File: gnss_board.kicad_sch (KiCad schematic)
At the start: 37 parts, among them J1 Conn_01x10_Pin, U1 H1102NL, U2 LAN8710A

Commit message: Schematic of the power supply with footprings
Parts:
- added C10: 2.2uF, symbol Device:C_Small
- added C11, C13, C14, C9: 100nF, symbol Device:C_Small
- added C12, C8: 22uF, symbol Device:C_Small
- added C15: 22uF/6.3V/20%/X5R/C0603, OLIMEX_RLC-FP:C_0603_5MIL_DWS, symbol ESP32-PoE_Rev_L1:C
- added C16: 12pF, Capacitor_SMD:C_0805_2012Metric, symbol Device:C_Small
- added C17: 470uF, Capacitor_THT:CP_Radial_D6.3mm_P2.50mm, symbol Device:C_Polarized
- added C18: 100nF, Capacitor_SMD:C_0805_2012Metric, symbol Device:C_Small
- added C19: 220pF, Capacitor_SMD:C_0805_2012Metric, symbol Device:C_Small
- added C7: 15uF, Capacitor_THT:CP_Radial_D6.3mm_P2.50mm, symbol Device:C_Polarized
- added D3: SS510, symbol Device:D_Schottky
- added FET1: WPM2015-3/TR, OLIMEX_Transistors-FP:SOT23, symbol ESP32-PoE_Rev_L1:P-MOS+DIOD
- added L2: 33uH, gnss_board:INDPM120120X800N, symbol Device:L
- added R21, R22: 4.42K, symbol Device:R
- added R23: 24.9K, symbol Device:R
- added R24: 0.03R, Resistor_SMD:R_1206_3216Metric, symbol Device:R
- added R25: 4.7K, Resistor_SMD:R_2512_6332Metric, symbol Device:R
- added R26: 10k/R0402, OLIMEX_RLC-FP:R_0402_5MIL_DWS, symbol ESP32-PoE_Rev_L1:R
- added R27: 1k/R0402, OLIMEX_RLC-FP:R_0402_5MIL_DWS, symbol ESP32-PoE_Rev_L1:R
- added R28: 301K, Resistor_SMD:R_0805_2012Metric, symbol Device:R
- added R29: 95.3K, Resistor_SMD:R_0805_2012Metric, symbol Device:R
- added R30: 4.7R, Resistor_SMD:R_0805_2012Metric, symbol Device:R
- added R31: 22R, Resistor_SMD:R_0805_2012Metric, symbol Device:R
- added T1: LMUN2211LT1G(SOT-23), OLIMEX_Transistors-FP:SOT23, symbol ESP32-PoE_Rev_L1:LMUN2211LT1G(SOT-23)
- added U3: TPS2375D, GNSS Board:SOIC127P599X175-8N, symbol gnss_board:TPS2375D
- added U4: TX4138(ESOIC-8), Package_SO:SOIC-8-1EP_3.9x4.9mm_P1.27mm_EP2.29x3mm_ThermalVias, symbol gnss_board:TX4138(ESOIC-8)
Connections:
- net +3.3VLAN: now also U2.12 (VDDIO), C8.1, C9.2, FET1.3
- net GND: now also C10.1, C11.1, C12.1, C13.1, C14.1, C17.2, C19.2, C7.2, C8.2, C9.1, D3.2 (A), R25.2, R29.2, T1.2 (E), U3.5 (RTN), U4.4 (GND)
- net VDD1A: now also U2.1 (VDD2A), U2.27 (VDD1A), C12.2, C13.2, C14.2
- net VIN+: now also C7.1, R23.2, R24.1, R25.1, U3.8 (VDD), U4.3 (Vin)
- net VIN-: now also R21.2, R22.2, U3.4 (VSS)
- net at U2.6 (VDDCR): now also C10.2, C11.2
- new net: R30.1, U4.8 (BS)
- new net: C18.1, R30.2
- new net: C18.2, D3.1 (K), L2.1, R31.1, U4.1 (SW)
- new net: R24.2, U4.2 (ILIM), U4.9 (ILIM)
- new net: C16.2, R28.2, R29.1, U4.5 (FB)
- new net: R21.1, U3.2 (CLASS)
- new net: C19.1, R31.2
- new net: R22.1, U3.1 (ILIM)
- new net: C15.2, FET1.1, R26.2, R27.1
- new net: R23.1, U3.3 (DET)
- new net: R27.2, T1.3 (C)
- new net +3.3V: C15.1, C16.1, C17.1, FET1.2, L2.2, R26.1, R28.1
- new net GPIO12\PHY_PWR: T1.1 (B)
- new net PSU_EN: U3.6 (PG), U4.6 (EN)
- no-connect marks 11 -> 13
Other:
- note added: "PoE PDC"
- note added: "Power Supply"
- moved on the sheet: C6, D5, D6, R10, R11, R12, R13, R14, R15, R16, R17, R18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

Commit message: Slowly grinding
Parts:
- R21: footprint (none) -> Resistor_SMD:R_0805_2012Metric; Info (none) -> 1%/R0805
- R22: value 4.42K -> 180K; footprint (none) -> Resistor_SMD:R_0805_2012Metric; Info (none) -> 1%/R0805
- R23: Info (none) -> 1%/R0805
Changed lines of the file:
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@@
 	)
 	(junction
-		(at 69.85 130.81)
-		(diameter 0)
-		(color 0 0 0 0)
-	)
-	(junction
 		(at 100.33 33.02)
 		(diameter 0)
@@
 	)
 	(junction
+		(at 71.12 130.81)
+		(diameter 0)
+		(color 0 0 0 0)
+	)
+	(junction
+		(at 71.12 146.05)
+		(diameter 0)
+		(color 0 0 0 0)
+	)
+	(junction
 		(at 335.28 30.48)
 		(diameter 0)
@@
 	)
 	(junction
-		(at 69.85 146.05)
-		(diameter 0)
-		(color 0 0 0 0)
-	)
-	(junction
 		(at 257.81 45.72)
 		(diameter 0)
@@
 	(wire
 		(pts
-			(xy 55.88 146.05) (xy 69.85 146.05)
+			(xy 55.88 146.05) (xy 71.12 146.05)
 		)
 		(stroke
@@
 	(wire
 		(pts
-			(xy 67.31 125.73) (xy 69.85 125.73)
+			(xy 67.31 125.73) (xy 71.12 125.73)
 		)
 		(stroke
@@
 	(wire
 		(pts
-			(xy 69.85 125.73) (xy 69.85 130.81)
+			(xy 71.12 125.73) (xy 71.12 130.81)
 		)
 		(stroke
@@
 	(wire
 		(pts
-			(xy 69.85 130.81) (xy 69.85 146.05)
+			(xy 71.12 130.81) (xy 71.12 146.05)
 		)
 		(stroke
@@
 	(wire
 		(pts
-			(xy 69.85 146.05) (xy 76.2 146.05)
-		)
-		(stroke
-			(width 0)
-			(type default)
-		)
-	)
-	(wire
-		(pts
 			(xy 48.26 43.18) (xy 53.34 43.18)
 		)
@@
 	(wire
 		(pts
-			(xy 67.31 130.81) (xy 69.85 130.81)
+			(xy 67.31 130.81) (xy 71.12 130.81)
 		)
 		(stroke
@@
 	(wire
 		(pts
+			(xy 71.12 146.05) (xy 76.2 146.05)
+		)
+		(stroke
+			(width 0)
+			(type default)
+		)
+	)
+	(wire
+		(pts
 			(xy 54.61 59.69) (xy 54.61 54.61)
 		)
@@
 			(effects
 				(font
-					(size 1.27 1.27)
+					(size 1 1)
 				)
 			)
 		)
-		(property "Footprint" ""
+		(property "Footprint" "Resistor_SMD:R_0805_2012Metric"
 			(at 63.5 127.508 90)
 			(effects
@@
 			)
 		)
+		(property "Info" "1%/R0805"
+			(at 68.326 124.968 90)
+			(effects
+				(font
+					(size 0.5 0.5)
+				)
+			)
+		)
 		(pin "2"
 		)
@@
 			)
 		)
-		(property "Value" "4.42K"
+		(property "Value" "180K"
 			(at 63.5 130.81 90)
 			(effects
 				(font
-					(size 1.27 1.27)
+					(size 1 1)
 				)
 			)
 		)
-		(property "Footprint" ""
+		(property "Footprint" "Resistor_SMD:R_0805_2012Metric"
 			(at 63.5 132.588 90)
 			(effects
@@
 			)
 		)
+		(property "Info" "1%/R0805"
+			(at 68.326 130.048 90)
+			(effects
+				(font
+					(size 0.5 0.5)
+				)
+			)
+		)
 		(pin "2"
 		)
@@
 			(effects
 				(font
-					(size 1.27 1.27)
+					(size 1 1)
 				)
 			)
@@
 			)
 		)
+		(property "Info" "1%/R0805"
+			(at 68.326 127.508 90)
+			(effects
+				(font
+					(size 0.5 0.5)
+				)
+			)
+		)

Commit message: Add footprints and arange components around
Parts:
- C1, C2, C3, C4: footprint (none) -> Capacitor_SMD:C_1206_3216Metric
- C10, C11, C12, C13: footprint (none) -> Capacitor_SMD:C_0805_2012Metric; Info (none) -> 10%/C0805
- C14, C9: footprint (none) -> Capacitor_SMD:C_0805_2012Metric; Info (none) -> 16V/10%/C0805
- C15: value 22uF/6.3V/20%/X5R/C0603 -> 22uF; footprint OLIMEX_RLC-FP:C_0603_5MIL_DWS -> Capacitor_SMD:C_0805_2012Metric; Fieldname 1 Value 1 -> (none); Fieldname2 Value2 -> (none); Fieldname3 Value3 -> (none); Info (none) -> 6.3V/20%/C0805
- C6: footprint (none) -> Capacitor_SMD:C_0805_2012Metric; Info (none) -> 6.3V/20%/C0805
- C8: footprint (none) -> Capacitor_SMD:C_0805_2012Metric; Field5 (none) -> 6.3V/20%/C0805
- D1: footprint MB10S:SOIC245P670X290-4N -> GNSS Board:SOIC245P670X290-4N
- D2: footprint MB10S:SOIC245P670X290-4N -> gnss_board:SOIC245P670X290-4N
- D5: Info (none) -> Yellow/D0805
- D6: footprint (none) -> LED_SMD:LED_0805_2012Metric; Info (none) -> Green/D0805
- FET1: footprint OLIMEX_Transistors-FP:SOT23 -> Package_TO_SOT_SMD:SOT-23_Handsoldering
- J1: footprint (none) -> Connector_JST:JST_SH_BM10B-SRSS-TB_1x10-1MP_P1.00mm_Vertical
- L1: value FB0805/600R/2A -> FB0805; footprint OLIMEX_RLC-FP:L_0805_5MIL_DWS -> Inductor_SMD:L_0805_2012Metric_Pad1.15x1.40mm_HandSolder; Fieldname 1 Value 1 -> (none); Fieldname2 Value2 -> (none); Fieldname3 Value3 -> (none); Info (none) -> 600R/2A
- R1, R2, R3, R4: footprint (none) -> Resistor_SMD:R_0805_2012Metric; Info 75V/100mW/0603/C4275 -> 1%/R0805
- R10, R12, R13, R14, R15, R16, R17, R18, R19, R9: value R -> 2.2K; footprint (none) -> Resistor_SMD:R_0805_2012Metric; Info (none) -> 5%/R0805
- R11: footprint (none) -> Resistor_SMD:R_0805_2012Metric; Info (none) -> 1%/R0805
- R20: footprint (none) -> Resistor_SMD:R_0805_2012Metric; Info (none) -> 5%/R0805
- R26: value 10k/R0402 -> 10k; footprint OLIMEX_RLC-FP:R_0402_5MIL_DWS -> Resistor_SMD:R_0805_2012Metric; Fieldname 1 Value 1 -> (none); Fieldname2 Value2 -> (none); Fieldname3 Value3 -> (none); Info (none) -> 5%/R0805
- R27: value 1k/R0402 -> 1K; footprint OLIMEX_RLC-FP:R_0402_5MIL_DWS -> Resistor_SMD:R_0805_2012Metric; Fieldname 1 Value 1 -> (none); Fieldname2 Value2 -> (none); Fieldname3 Value3 -> (none); Info (none) -> 5%/R0805
- R5, R6, R7, R8: footprint (none) -> Resistor_SMD:R_0805_2012Metric; Info 75V/100mW/0603/C4275 -> 75V/100mW/0805
- T1: value LMUN2211LT1G(SOT-23) -> LMUN2211LT1G; footprint OLIMEX_Transistors-FP:SOT23 -> Package_TO_SOT_SMD:SOT-23_Handsoldering
- TVS1: value ESDS314DBVR(SOT-23-5) -> ESDS314DBVR
- TVS2, TVS3: value D_TVS -> GG0603052R542P; footprint (none) -> Diode_SMD:D_0603_1608Metric; Info (none) -> GG0603052R542P
- U1: footprint H11X_PUL -> GNSS Board:H11X_PUL
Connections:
- net +3.3V: now also C15.2, R26.2; no longer C15.1, R26.1
- net +3.3VLAN: now also C9.1; no longer C9.2
- net GND: now also C9.2; no longer C9.1
- net at R27.2: now also C15.1, FET1.1, R26.1; no longer T1.3 (C)
- net GPIO12\PHY_PWR renamed PHY_PWR
- new net: R27.1, T1.3 (C)
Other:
- note added: "ETH Power Switch"
- moved on the sheet: C10, C11, C12, C13, C14, C15, C16, C17, C18, C19, C6, C7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

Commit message: Update connector
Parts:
- J1: footprint Connector_JST:JST_SH_BM10B-SRSS-TB_1x10-1MP_P1.00mm_Vertical -> Connector_Molex:Molex_PicoBlade_53398-1071_1x10-1MP_P1.25mm_Vertical
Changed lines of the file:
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@@
 			)
 		)
-		(property "Footprint" "Connector_JST:JST_SH_BM10B-SRSS-TB_1x10-1MP_P1.00mm_Vertical"
+		(property "Footprint" "Connector_Molex:Molex_PicoBlade_53398-1071_1x10-1MP_P1.25mm_Vertical"
 			(at 20.32 52.07 0)
 			(effects

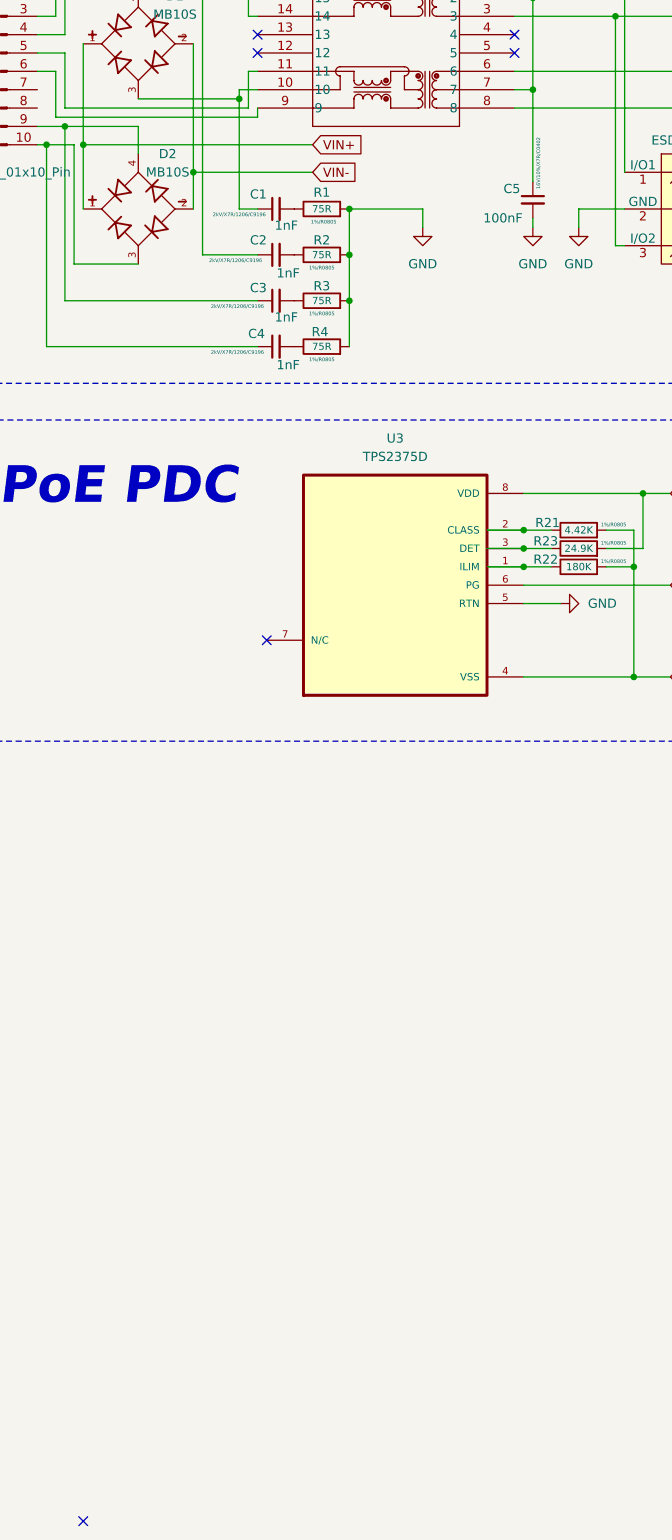
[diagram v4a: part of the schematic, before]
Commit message: Add power supply to ESP32
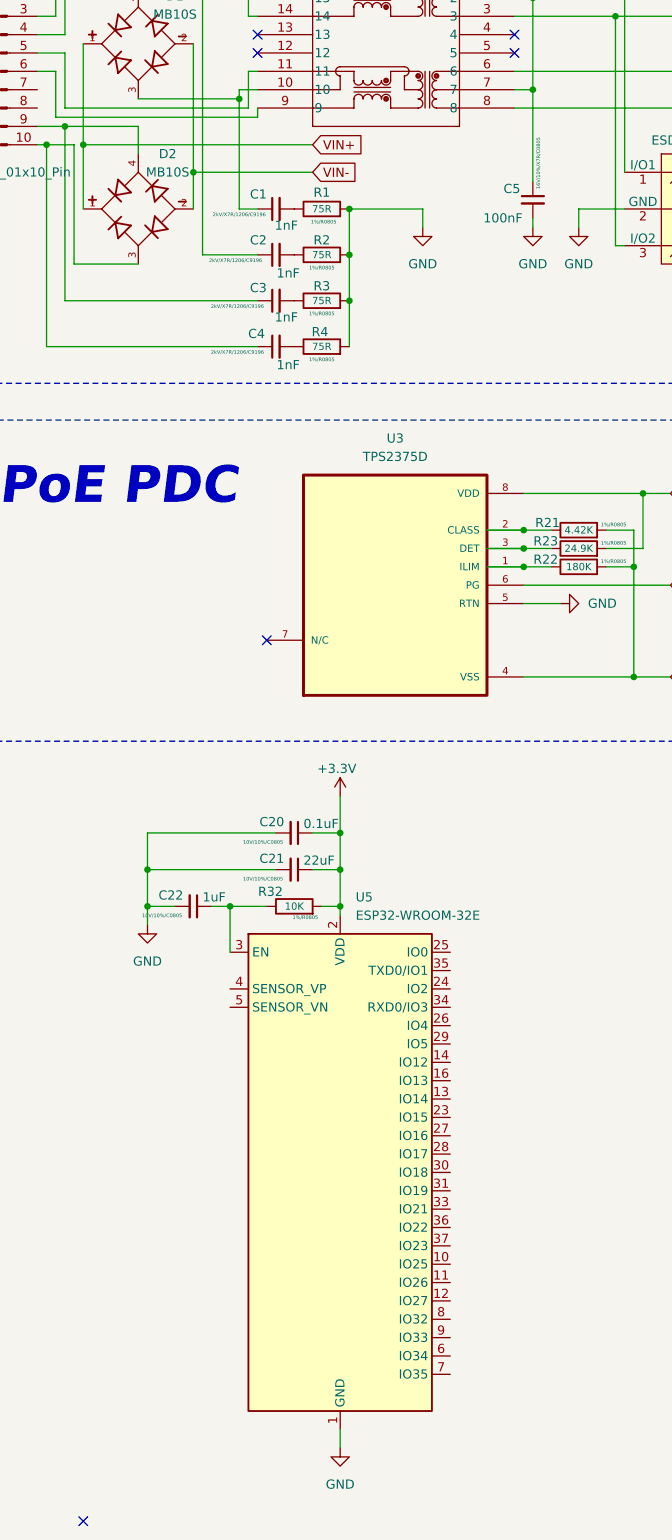
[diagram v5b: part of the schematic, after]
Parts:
- added C20: 0.1uF, Capacitor_SMD:C_0805_2012Metric, symbol Device:C_Small
- added C21: 22uF, Capacitor_SMD:C_0805_2012Metric, symbol Device:C_Small
- added C22: 1uF, Capacitor_SMD:C_0805_2012Metric, symbol Device:C_Small
- added R32: 10K, Resistor_SMD:R_0805_2012Metric, symbol Device:R
- added U5: ESP32-WROOM-32E, RF_Module:ESP32-WROOM-32D, symbol RF_Module:ESP32-WROOM-32E
- C5: footprint (none) -> Capacitor_SMD:C_0805_2012Metric; Info 16V/10%/X7R/C0402 -> 16V/10%/X7R/C0805
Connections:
- net +3.3V: now also C20.1, C21.1, R32.2, U5.2 (VDD)
- net GND: now also C20.2, C21.2, C22.2, U5.1 (GND), U5.15 (GND), U5.38 (GND), U5.39 (GND)
- new net: C22.1, R32.1, U5.3 (EN)

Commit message: Connect ESP32 to the LAN chip
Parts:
- added R33: 10K, Resistor_SMD:R_0805_2012Metric, symbol Device:R
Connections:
- net CLK_OUT is gone; now on net ETH_CLK_IN: U2.5 (XTAL1/CLKIN)
- net MDC is gone; now on net ETH_MDC: U2.17 (MDC)
- net MDIO is gone; now on net ETH_MDIO: R19.1, U2.16 (MDIO)
- net PHY_PWR is gone; now on net ETH_PHY_PWR: T1.1 (B)
- net RXD0 is gone; now on net ETH_RXD0: R12.1, U2.11 (RXD0/~{MODE0})
- net RXD1 is gone; now on net ETH_RXD1: R13.1, U2.10 (RXD1/~{MODE1})
- net RX_CRS_DV is gone; now on net ETH_RX_CRS_DV: R18.1, U2.15 (COL/CRS_DV/~{MODE2})
- net TXD0 is gone; now on net ETH_TXD0: U2.22 (TXD0)
- net TXD1 is gone; now on net ETH_TXD1: U2.23 (TXD1)
- net TX_EN is gone; now on net ETH_TX_EN: U2.21 (TXEN)
- net +3.3V: now also R33.1
- net ESP_EN: now reaches C22.1, R32.1, U5.3 (EN)
- net ETH_RXD0: now reaches U5.10 (IO25)
- net ETH_RXD1: now reaches U5.11 (IO26)
- net ETH_RX_CRS_DV: now reaches U5.12 (IO27)
- net ETH_PHY_PWR: now reaches U5.14 (IO12)
- net ESP_IO0: now reaches U5.25 (IO0)
- net ESP_IO0: now also R33.2
- net ETH_CLK_IN: now reaches U5.28 (IO17)
- net ETH_MDIO: now reaches U5.30 (IO18)
- net ETH_TXD0: now reaches U5.31 (IO19)
- net ETH_TX_EN: now reaches U5.33 (IO21)
- net ESP_RXD0: now reaches U5.34 (RXD0/IO3)
- net ESP_TXD0: now reaches U5.35 (TXD0/IO1)
- net ETH_TXD1: now reaches U5.36 (IO22)
- net ETH_MDC: now reaches U5.37 (IO23)

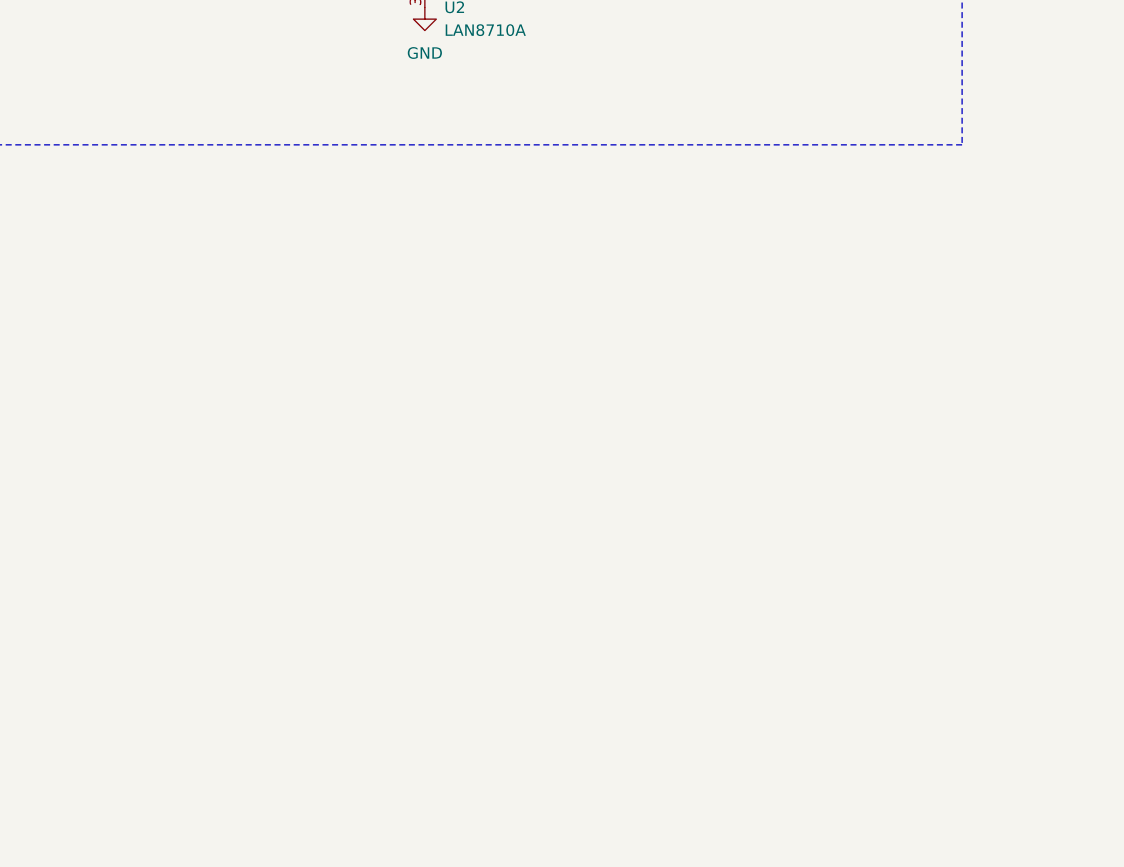
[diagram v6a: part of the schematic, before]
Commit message: Add Serial Connector for programming
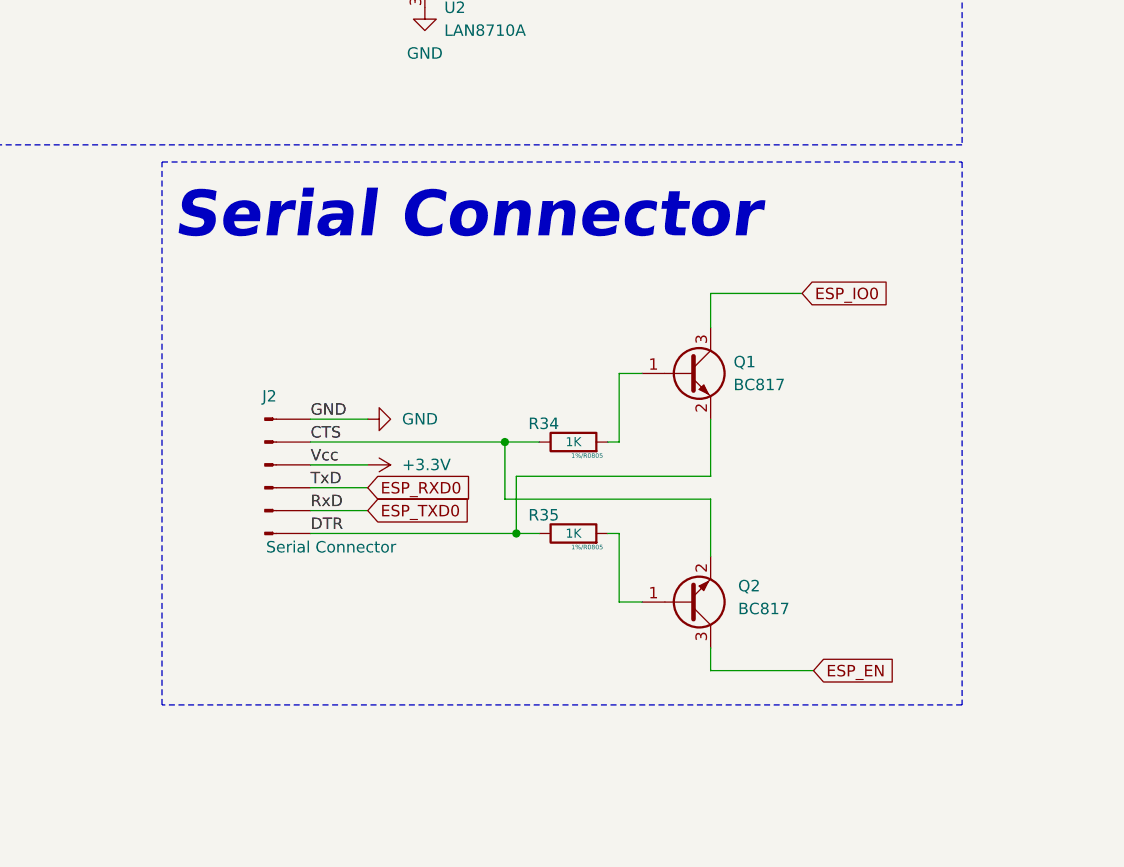
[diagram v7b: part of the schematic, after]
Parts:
- added J2: Serial Connector, Connector_PinHeader_2.54mm:PinHeader_1x06_P2.54mm_Vertical, symbol Connector:Conn_01x06_Pin
- added Q1, Q2: BC817, Package_TO_SOT_SMD:SOT-23, symbol Transistor_BJT:BC817
- added R34, R35: 1K, Resistor_SMD:R_0805_2012Metric, symbol Device:R
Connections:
- net +3.3V: now also J2.3 (Pin_3)
- net ESP_EN: now also Q2.3 (C)
- net ESP_IO0: now also Q1.3 (C)
- net ESP_RXD0: now also J2.4 (Pin_4)
- net ESP_TXD0: now also J2.5 (Pin_5)
- net GND: now also J2.1 (Pin_1)
- new net: Q1.1 (B), R34.2
- new net: Q2.1 (B), R35.2
- new net CTS: J2.2 (Pin_2), Q2.2 (E), R34.1
- new net DTR: J2.6 (Pin_6), Q1.2 (E), R35.1
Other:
- note added: "Serial Connector"

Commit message: Add SparkFun Symbols & Footprints
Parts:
- added U6: UM980, SparkFun-GPS:UM980, symbol SparkFun-GPS:UM980
- U1: footprint GNSS Board:H11X_PUL -> gnss_board:H11X_PUL
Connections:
- net GND: now also U6.1 (GND), U6.100 (GND), U6.101 (GND), U6.102 (GND), U6.12 (GND), U6.14 (GND), U6.3 (GND), U6.32 (GND), U6.37 (GND), U6.41 (GND), U6.48 (GND), U6.55 (GND), U6.56 (GND), U6.57 (GND), U6.58 (GND), U6.59 (GND), U6.60 (GND), U6.61 (GND), U6.62 (GND), U6.63 (GND), U6.64 (GND), U6.65 (GND), U6.66 (GND), U6.67 (GND), U6.68 (GND), U6.69 (GND), U6.70 (GND), U6.71 (GND), U6.72 (GND), U6.73 (GND), U6.74 (GND), U6.75 (GND), U6.76 (GND), U6.77 (GND), U6.78 (GND), U6.79 (GND), U6.80 (GND), U6.81 (GND), U6.82 (GND), U6.83 (GND), U6.84 (GND), U6.85 (GND), U6.86 (GND), U6.87 (GND), U6.88 (GND), U6.89 (GND), U6.90 (GND), U6.91 (GND), U6.92 (GND), U6.93 (GND), U6.94 (GND), U6.95 (GND), U6.96 (GND), U6.97 (GND), U6.98 (GND), U6.99 (GND)
- new net: U6.13 (NC), U6.15 (NC), U6.16 (NC), U6.17 (NC), U6.18 (NC), U6.22 (NC), U6.23 (NC), U6.24 (NC), U6.25 (NC), U6.35 (NC), U6.38 (NC), U6.39 (NC), U6.40 (NC), U6.46 (NC), U6.47 (NC), U6.50 (NC), U6.52 (NC), U6.54 (NC)
- new net VCC: U6.33 (VCC), U6.34 (VCC)
- no-connect marks 13 -> 12
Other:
- note added: "ESP32-WROOM-32E"
- moved on the sheet: C20, C21, C22, R32, R33, U5
